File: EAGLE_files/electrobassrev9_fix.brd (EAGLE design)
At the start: 314.7 x 129.5 mm, 283 parts, among them IC1 LMV324M, IC18 CY8C4124, IC2 4052D, IC3 LMV321M5, IC5 LMV321M5, J1 105162-0001, J2 SM06B-SRSS-TB(LF)(SN), J28 PJ-066A, J3 SM06B-SRSS-TB(LF)(SN), J5 SM06B-SRSS-TB(LF)(SN), J6 SM06B-SRSS-TB(LF)(SN), J7 SM06B-SRSS-TB(LF)(SN), J8 SM06B-SRSS-TB(LF)(SN), Q1 DMP3099L, U1 ES_DAISY_SEED_DOUBLE, U10 OPA1654, U2 LP2985, U3 MCP1755T-5002E/DCSOT-223_5_MC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, U4 CY8C5888LTI-LP097QFN-68-M, U5 ADUM3160BRWZRW_16_ADI-M, U6 LSM6DSLTR, U7 ES_DAISY_SEED_DOUBLE, X1 3P-2MM-TH-MALE, X10 3P-2MM-TH-MALE, X11 3P-2MM-TH-MALE, X12 3P-2MM-TH-MALE, X13 3P-2MM-TH-MALE, X14 3P-2MM-TH-MALE, X15 3P-2MM-TH-MALE, X16 332-02, X17 332-02, X18 332-02, X19 332-02, X2 NRJ6HF2, X3 NRJ6HF2, X4 USB+SHIELD, X5 332-02, X6 332-02, X7 332-02, X8 332-02, X9 3P-2MM-TH-MALE

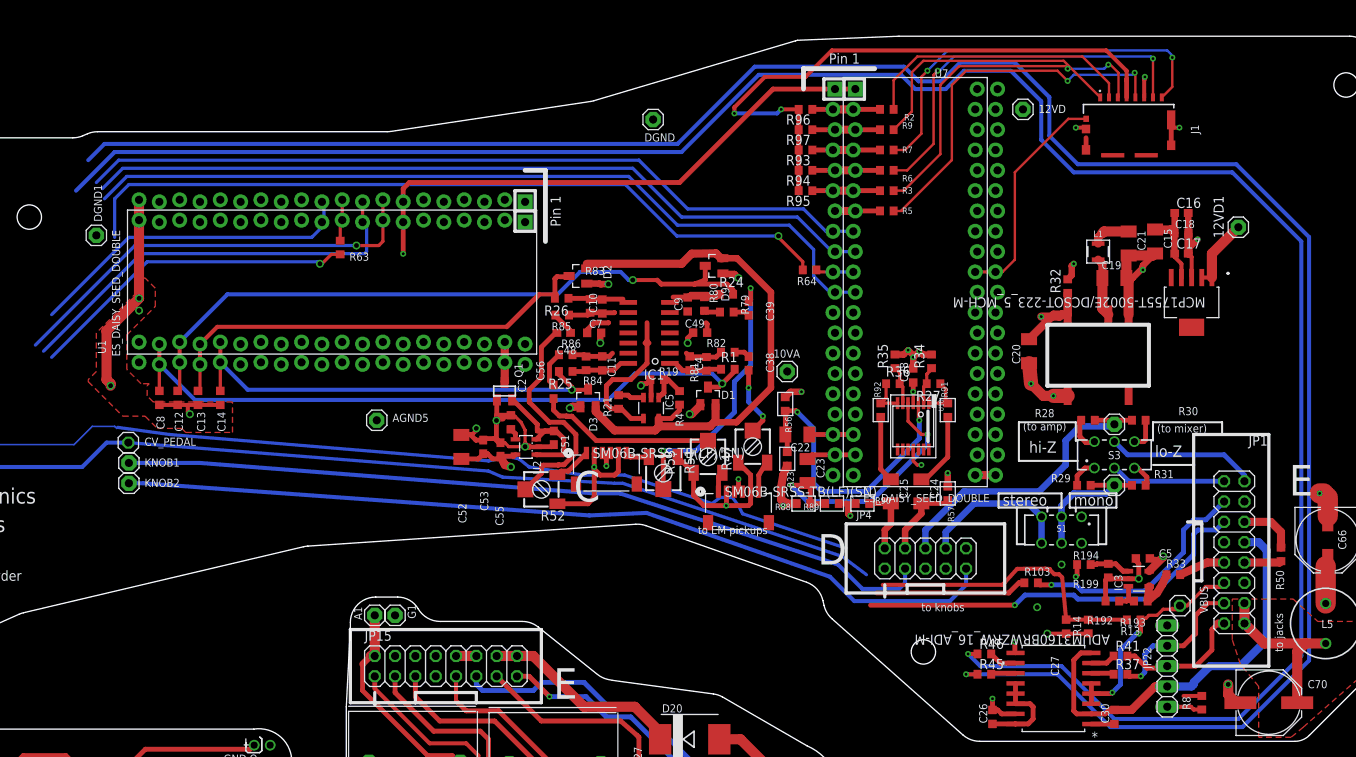
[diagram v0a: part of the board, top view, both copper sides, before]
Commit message: updated eagle file for rev9 fix
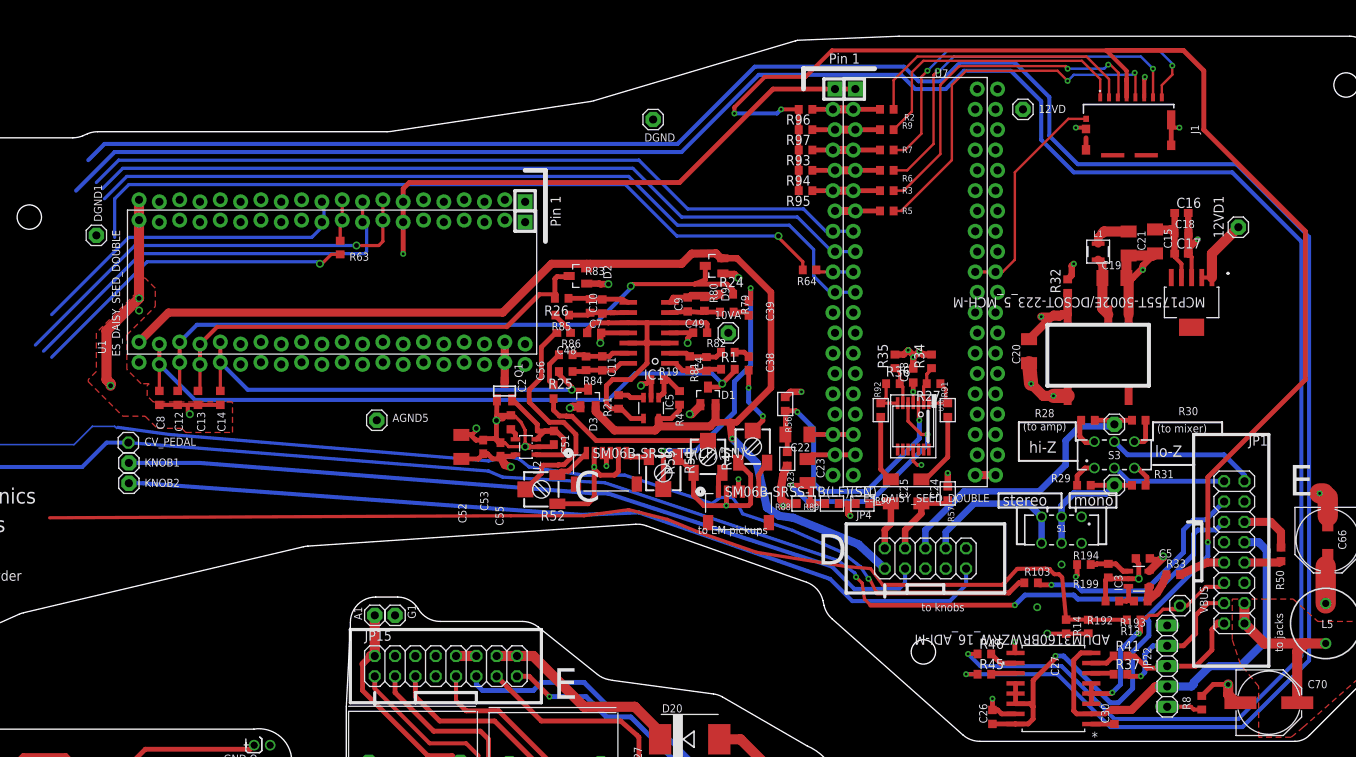
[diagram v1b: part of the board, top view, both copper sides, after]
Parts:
- moved 10VA 8.81 mm to (191.0, 70.4)
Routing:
- net +3V3: track 113.9 -> 239.0 mm, vias 6 -> 8
- net VBUS_DIVIDED: track 36.7 -> 143.0 mm
- net 3V3A1: track 100.5 -> 189.5 mm, vias 3 -> 4
- net 1.5V_MID: track 24.4 -> 41.3 mm
- net CV_PEDAL_SENSE: track 195.3 -> 201.8 mm, vias 1 -> 2
- net N$33: track 2.34 -> 6.44 mm
- net AGND: track 207.6 -> 210.9 mm
- net CV_PEDAL: track 231.9 -> 235.0 mm, vias 2 -> 3
- net +10V: track 16.2 -> 19.1 mm
- net N$35: track 5.82 -> 8.05 mm
- net N$30: track 6.92 -> 8.98 mm
- net N$34: track 5.26 -> 7.23 mm
- net DGND: track 86.7 -> 88.3 mm
- net DAT2: track 34.1 -> 35.5 mm
- net ADC2_1: track 83.7 -> 82.6 mm
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
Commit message: updated eagle file for rev9 fix
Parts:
- removed JP31: (no value), pinhead:1X02
- added C47: 1uf, rcl:C0603
- added C50, C54: .1uf, rcl:C0603K
- added JP7: (no value), pinhead:1X02
- added LED1: (no value), led:CHIP-LED0603
- added R54: 82R, adafruit:R0603
- added R55: 0R, adafruit:R0603
- added U8: MCP23008T-E/SS, MCP23008T-E_SS:SOP65P780X200-20N
- moved JP23 42.8 mm to (32.8, 67.6), turned to 90 degrees
- moved DGND1 10.00 mm to (107.4, 91.4)
- moved R49 5.59 mm to (61.0, 86.6), turned to 180 degrees
- moved C3 4.37 mm to (306.6, 76.7), turned to 90 degrees
- moved R60 4.33 mm to (38.9, 73.9), turned to 90 degrees
- moved R48 3.81 mm to (61.0, 84.3), turned to 180 degrees
- moved JP35 3.54 mm to (28.7, 83.3), turned to 270 degrees
- moved C33 2.05 mm to (52.1, 57.9)
- moved C31 1.93 mm to (60.5, 59.2)
- moved C32 1.80 mm to (50.0, 58.2)
- moved C42 1.80 mm to (48.3, 58.2)
- moved C41 1.78 mm to (54.1, 58.2)
- moved C36 1.05 mm to (64.5, 66.0)
- moved JP5 1.02 mm to (49.3, 84.3)
- moved R40 1.02 mm to (44.2, 73.4)
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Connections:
- net EDIT renamed ENTER
- removed net FRETTED_LATCHING: JP23.3, U4.47
- removed net FRETTED_MOMENTARY: JP23.4, U4.46
- removed net FR_LATCHING: JP24.3, S4.1
- removed net FR_MOMENTARY: JP24.4, S2.1
- removed net GND: U6.7
- removed net GND_2: U6.6
- removed net LED_1: JP23.10, U4.50
- removed net VDD: U6.8
- removed net VDDIO: U6.5
- new net ADC2BYPASS: C47.1, U4.50
- new net N$68: IC18.9, JP7.2
- new net N$69: IC18.10, JP7.1
- new net N$70: LED1.A, R54.1
- new net N$71: S2.1, U8.12
- new net N$72: S4.1, U8.13
- new net N$73: D13.A, U8.16
- new net N$74: R55.1, U6.1
- new net NECKSENSE1: JP2.9, U4.46
- new net NECKSENSE2: JP2.7, U4.47
- net +3V3: now also C50.1, C54.1, U6.12, U6.5, U6.8
- net AGND: now also C47.2; no longer JP1.6
- net AGND3: no longer JP15.8
- net BLUE_LED: now also R54.2
- net DGND: now also C50.2, C54.2, LED1.C, R55.2, U6.2, U6.3, U6.6, U6.7
- net DGND3: no longer JP37.1, R127.2, X4.GND
- net FR_3V3: now also U8.20
- net FR_GND: now also U8.9
- net GNDINT: now also JP1.6
- net N$43: now also U$13.P$1; no longer U$13.P$2
- net N$44: now also U$12.P$1; no longer U$12.P$2
- net N$47: now also JP15.8, JP37.1, R127.2, X4.GND; no longer D13.A, JP24.10
- net SCL: now also U6.13; no longer JP31.1
- net SCL_1: now also U8.1
- net SDA: now also U6.14; no longer JP31.2
- net SDA_1: now also U8.2
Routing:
- net USBDM: track 274.5 -> 393.3 mm, vias 1 -> 2
- net USBDP: track 273.8 -> 384.8 mm, vias 1 -> 2
- net SPI_READY: track 69.8 -> 176.8 mm, vias 1 -> 2
- net SCL: track 0.40 -> 104.0 mm, vias 0 -> 4
- net VBUS_DIVIDED: track 143.0 -> 234.2 mm, vias 0 -> 2
- net SDA: track 2.16 -> 92.5 mm, vias 0 -> 3
- net SCLK_1: track 52.1 -> 138.0 mm, vias 0 -> 1
- net DOWN: track 0.00 -> 85.0 mm, vias 0 -> 6
- net SS_2: track 99.5 -> 184.4 mm, vias 0 -> 3
- net MOSI_1: track 42.1 -> 124.9 mm, vias 0 -> 1
- net SCLK_2: track 99.7 -> 181.4 mm, vias 0 -> 1
- net KNOB_2: track 115.7 -> 193.9 mm, vias 0 -> 2
- net MISO_1: track 50.2 -> 128.2 mm
- net DGND: track 88.3 -> 165.5 mm, vias 12 -> 27
- net MOSI_2: track 102.9 -> 179.6 mm, vias 0 -> 1
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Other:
- outline, holes or cut-outs redrawn

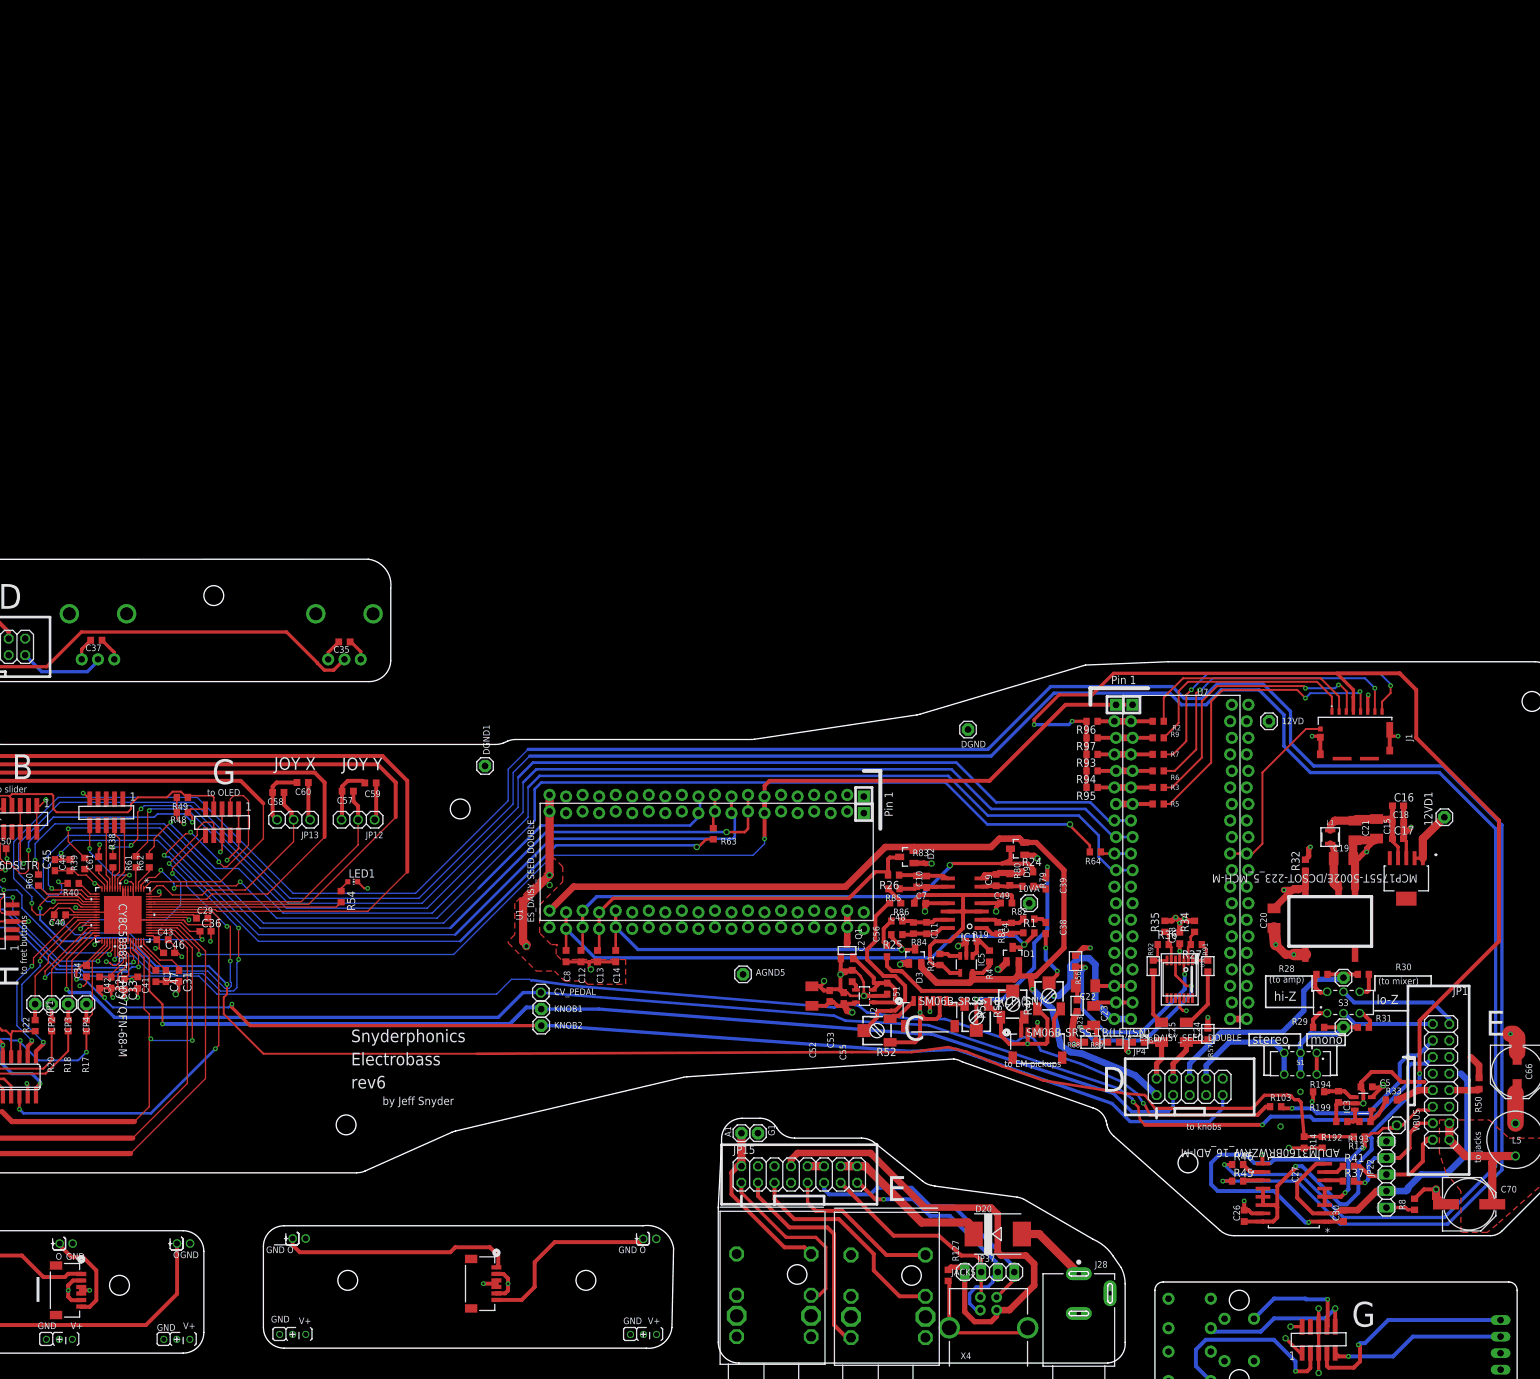
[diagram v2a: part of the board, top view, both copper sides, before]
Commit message: fixed reading of new presets from plugin to align with electrosteel
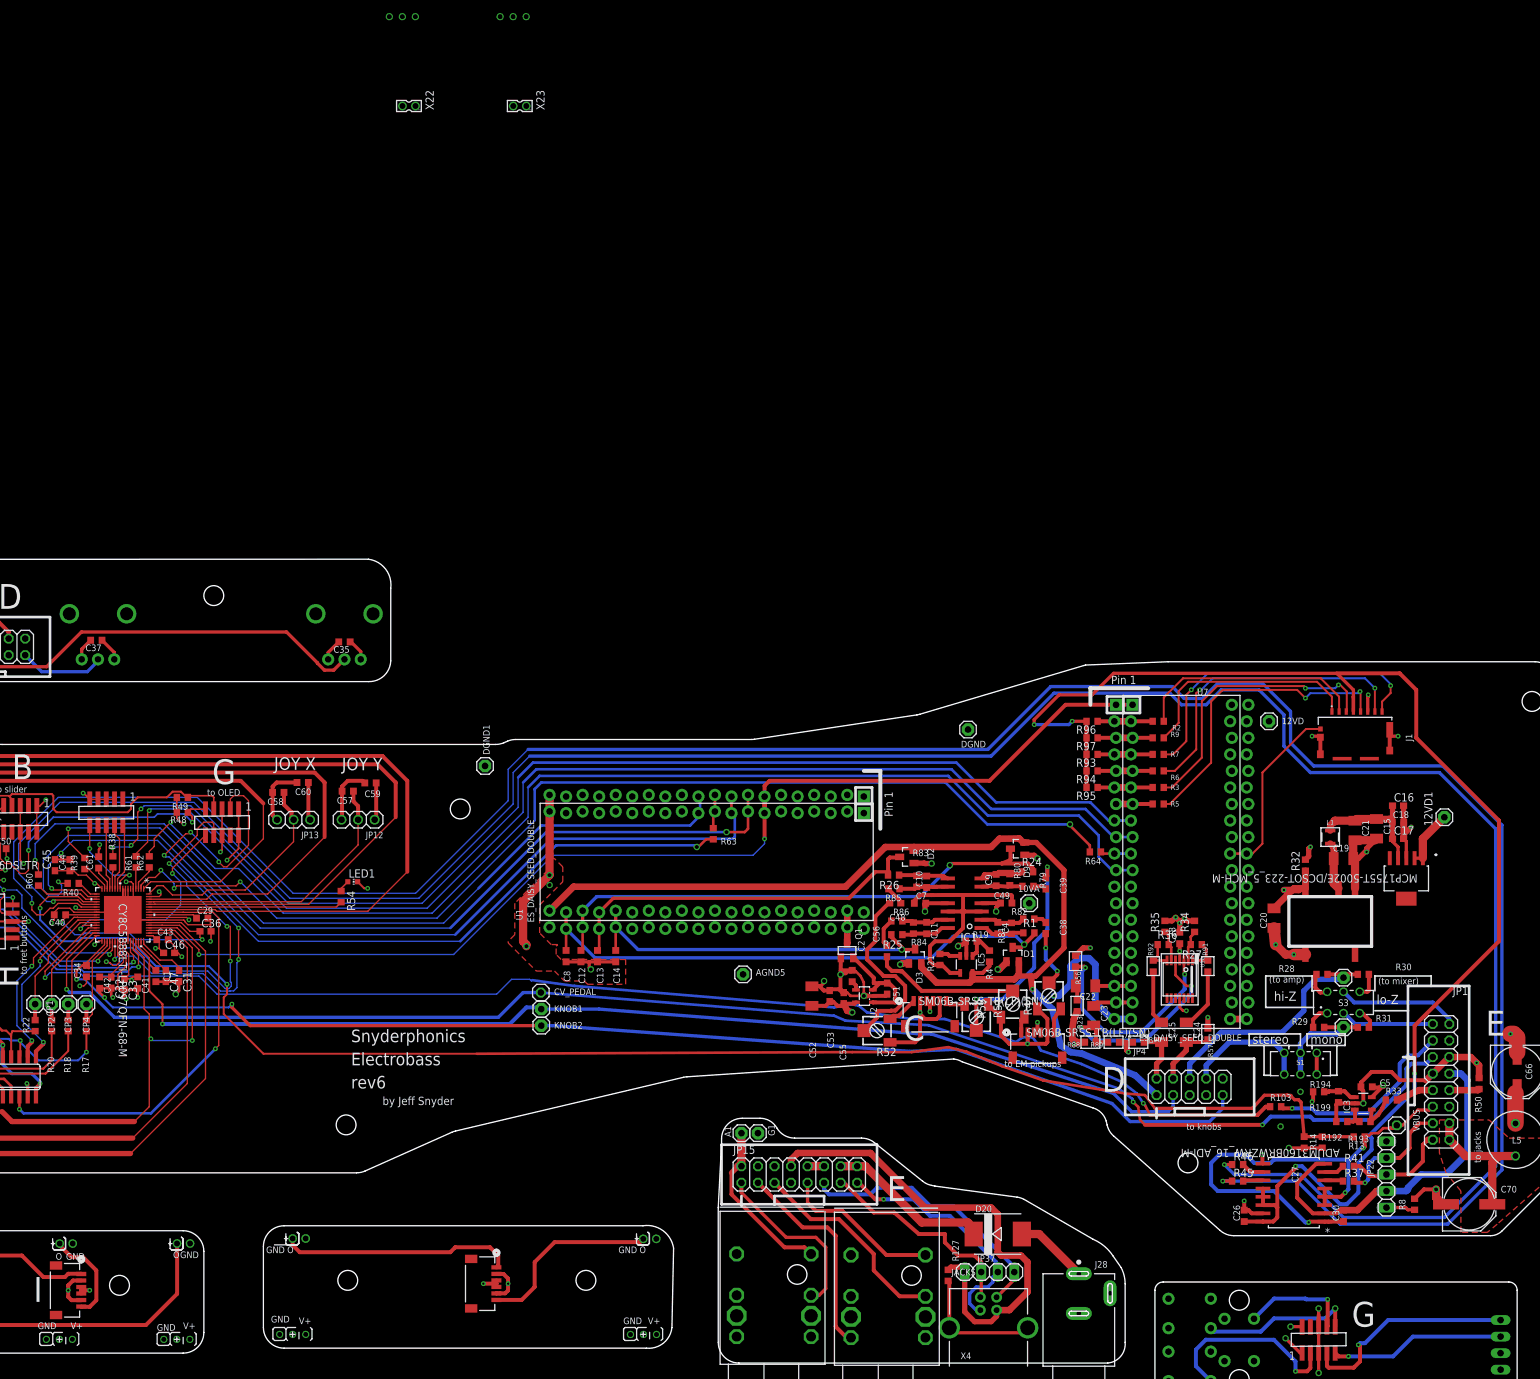
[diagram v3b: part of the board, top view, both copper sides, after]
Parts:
- added X20, X21: 3P-2MM-TH-MALE, CYCFI_Con:3P-2MM-TH
- added X22, X23: 332-02, con-garry:332-02
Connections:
- new net ELECTROSTEELHIGH: X20.P$3, X21.P$3
- new net ELECTROSTEEL_GND: X20.P$1, X20.P$2, X21.P$1, X21.P$2, X22.2, X23.2
- net AGND: now also JP1.6
- net AGND3: now also JP15.6
- net AGND4: no longer JP15.6
- net GNDINT: no longer JP1.6
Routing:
- net AGND: track 250.4 -> 258.9 mm, vias 30 -> 31
- net AGND3: track 0.00 -> 3.59 mm
- net GNDIO: track 51.5 -> 53.3 mm
- net N$55: track 33.4 -> 31.9 mm
- net N$47: track 76.1 -> 74.8 mm
- net N$122: track 33.5 -> 32.3 mm
- net N$58: track 32.1 -> 32.7 mm
- net DGND: track 165.5 -> 166.1 mm, vias 27 -> 26
- added copper zone on layer 2, net N$47
